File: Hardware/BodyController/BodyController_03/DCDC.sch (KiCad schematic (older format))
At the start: 57 parts, among them Q12 BUK9Y3R0-40E,115, Q13 BUK9Y3R0-40E,115, Q16 2N7002, Q6 NX1029X,115, Q7 NX1029X,115, U21 LM2903QDRQ1, U25 UCC27511A-Q1, U27 INA21x

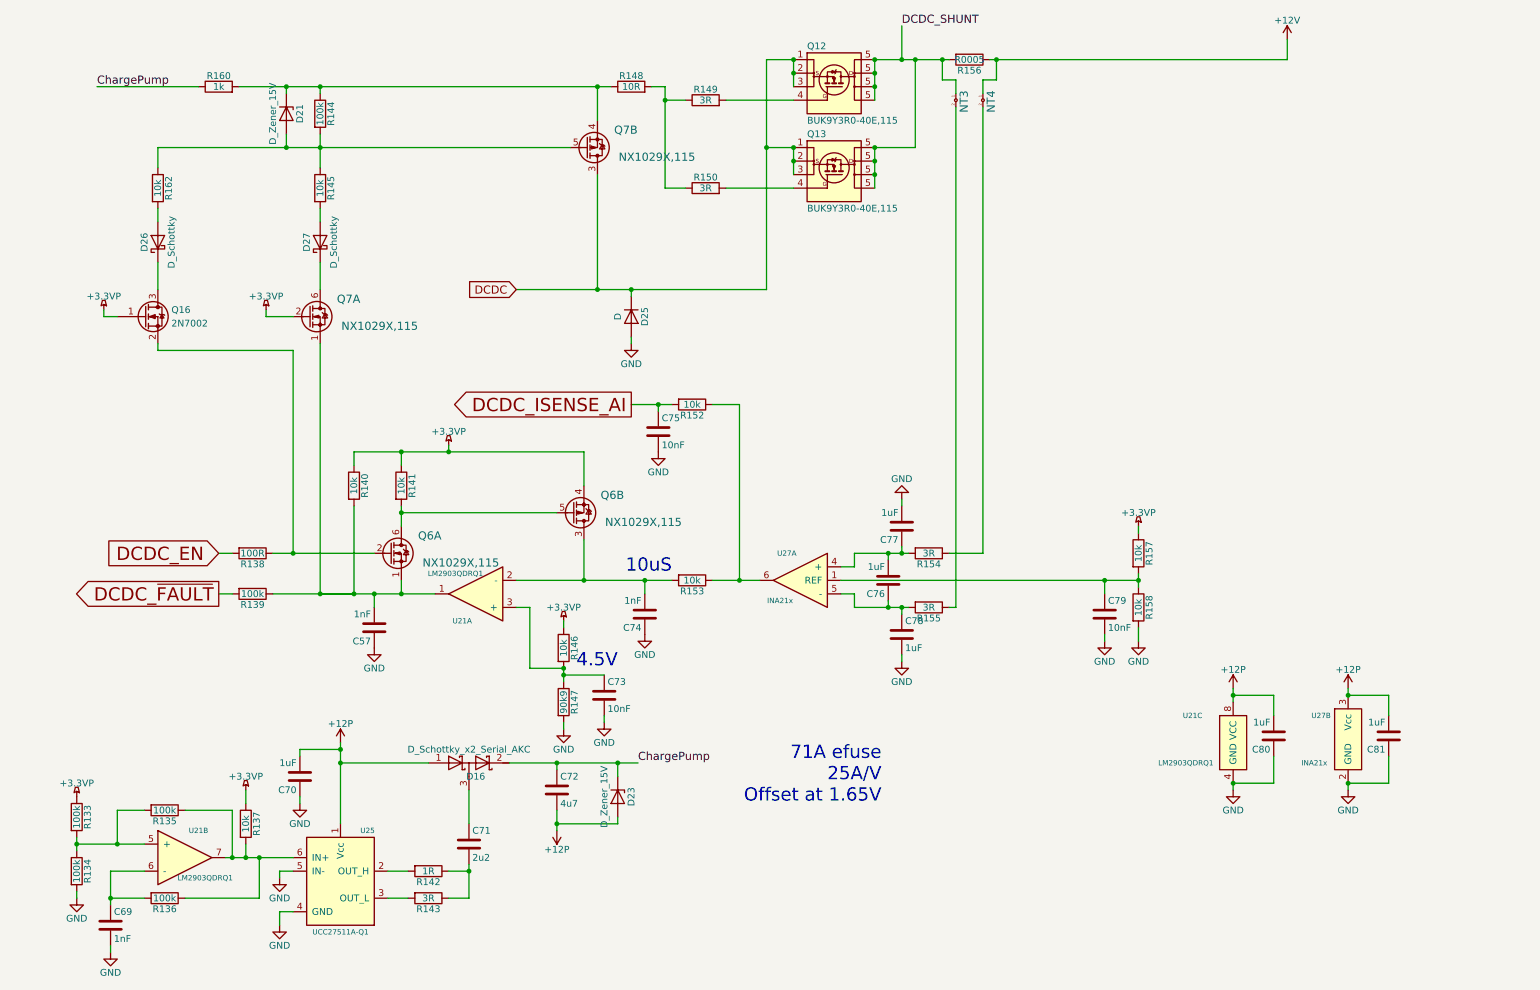
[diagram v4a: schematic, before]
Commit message: Added resistor values via BOM importer. Changed layout file to add large CAN resistors and buffer to 1.65V Reference
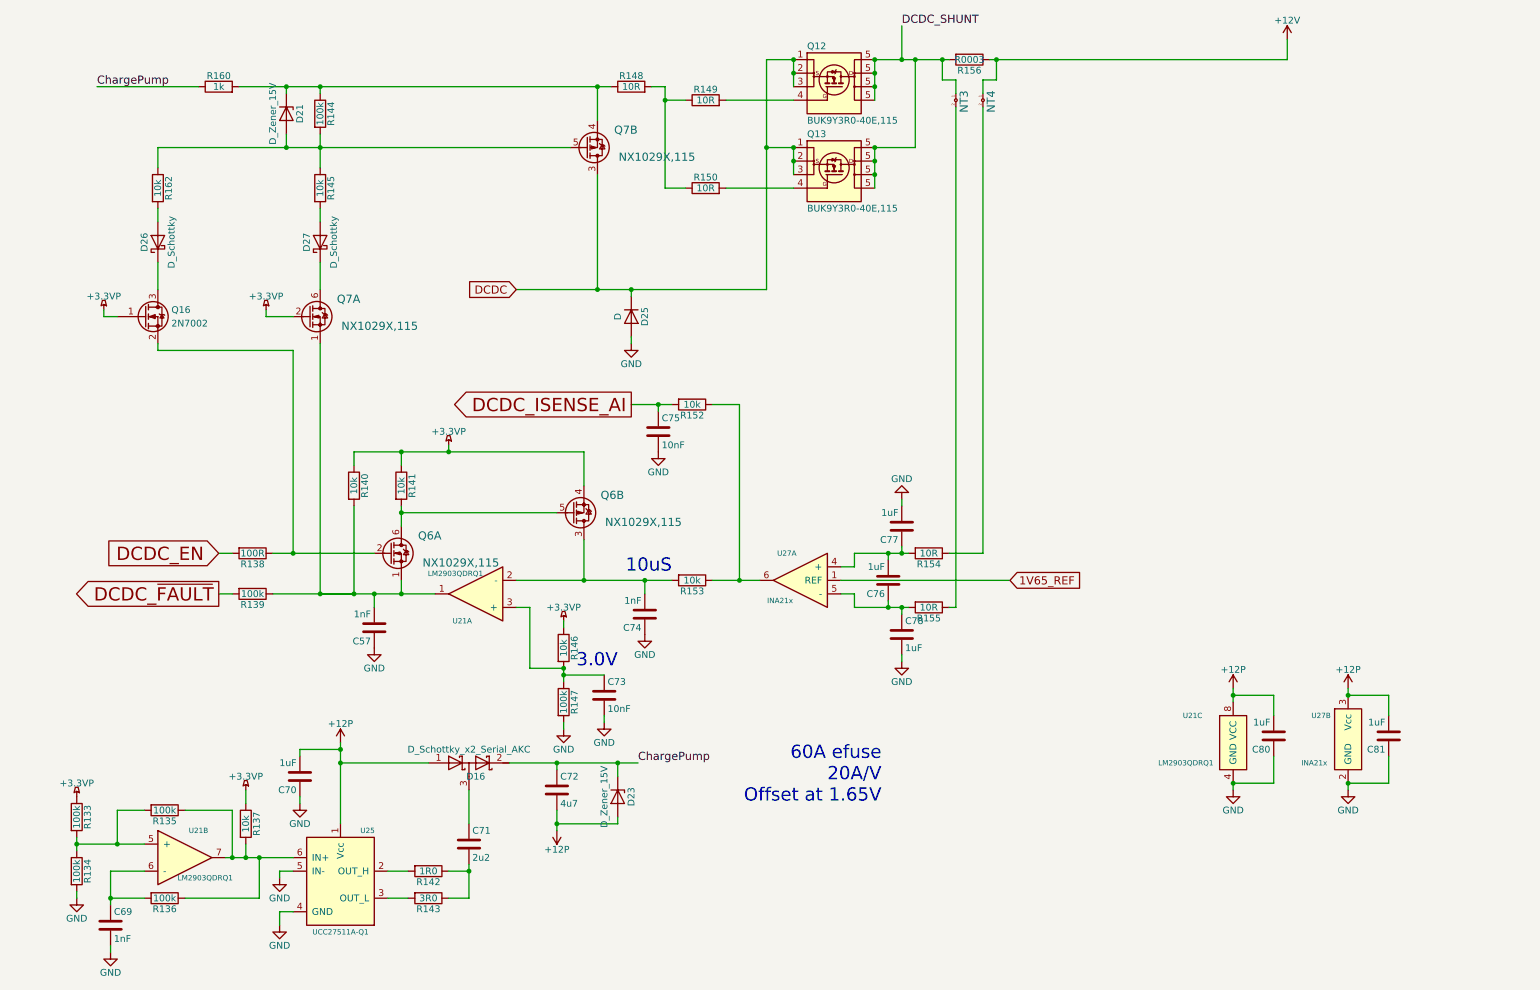
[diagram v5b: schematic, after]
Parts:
- removed C79: 10nF, Capacitors_SMD:C_0603, symbol C
- removed R157, R158: 10k, Resistors_SMD:R_0603, symbol R
- R133, R134, R135, R136, R139, R144: PartNumber (none) -> AC0603FR-07100KL
- R137, R140, R141, R145, R146, R152, R153, R162: PartNumber (none) -> AC0603FR-0710KL
- R138: PartNumber (none) -> AC0603FR-07100RL
- R142: value 1R -> 1R0; PartNumber (none) -> AC0603JR-071RL
- R143: value 3R -> 3R0; PartNumber (none) -> ERJ-3GEYJ3R0V
- R147: value 90k9 -> 100k; PartNumber (none) -> AC0603FR-07100KL
- R148: PartNumber (none) -> AC0603FR-0710RL
- R149, R150, R154, R155: value 3R -> 10R; PartNumber (none) -> AC0603FR-0710RL
- R156: value R0005 -> R0003; PartNumber (none) -> HCS2512FTL300
- R160: PartNumber (none) -> AC0603FR-071KL
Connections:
- net 1V65_REF: now reaches U27.1 (REF)
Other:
- note added: "3.0V"
- note added: "60A efuse\n20A/V\nOffset at 1.65V"
- note removed: "4.5V"
- note removed: "71A efuse\n25A/V\nOffset at 1.65V"
